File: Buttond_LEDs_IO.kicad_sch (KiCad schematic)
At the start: 16 parts, among them J14 Conn_01x04, J15 Conn_01x08, SW1 RESET, SW2 BOOT

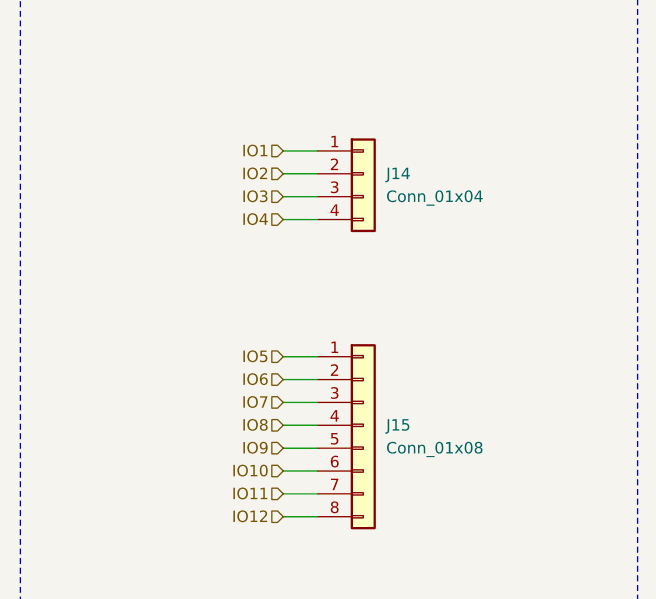
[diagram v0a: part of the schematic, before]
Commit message: moving to kicad-bild
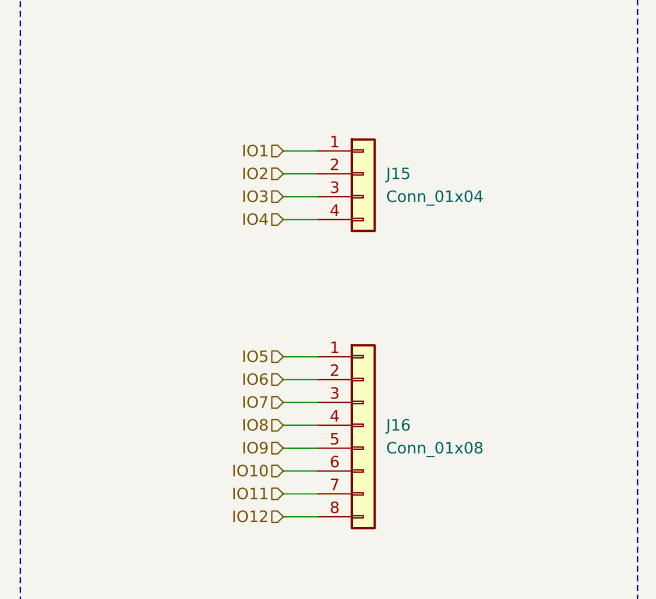
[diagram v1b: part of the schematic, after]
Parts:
- renumbered J14 to J15, J15 to J16
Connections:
- net BOOT: now also SW2.3 (B), SW2.4 (B); no longer SW2.2 (B)
- net GND: now also SW1.2 (A), SW2.2 (A)
- net Reset: now also SW1.3 (B), SW1.4 (B); no longer SW1.2 (B)
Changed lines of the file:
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@@
 		(dnp no)
 		(fields_autoplaced yes)
-		(property "Reference" "J15"
+		(property "Reference" "J16"
 			(at 247.65 90.8049 0)
 			(effects
@@
 			(project ""
 				(path "/795c8e51-3ded-4d21-b864-aaff31c5def7/6282503b-e4ab-454b-a074-f701a067f39b/cecfe08a-2de2-4171-9051-c68b429ab9e8"
-					(reference "J15")
+					(reference "J16")
 					(unit 1)
 				)
@@
 		(dnp no)
 		(fields_autoplaced yes)
-		(property "Reference" "#PWR059"
+		(property "Reference" "#PWR063"
 			(at 156.21 107.95 0)
 			(effects
@@
 			(project "VehicleControlUnit"
 				(path "/795c8e51-3ded-4d21-b864-aaff31c5def7/6282503b-e4ab-454b-a074-f701a067f39b/cecfe08a-2de2-4171-9051-c68b429ab9e8"
-					(reference "#PWR059")
+					(reference "#PWR063")
 					(unit 1)
 				)
@@
 			)
 		)
+		(property "Sim.Pins" "1=K 2=A"
+			(at 133.35 92.71 0)
+			(effects
+				(font
+					(size 1.27 1.27)
+				)
+				(hide yes)
+			)
+		)
 		(pin "1"
 		)
@@
 		(dnp no)
 		(fields_autoplaced yes)
-		(property "Reference" "J14"
+		(property "Reference" "J15"
 			(at 247.65 62.8649 0)
 			(effects
@@
 			(project ""
 				(path "/795c8e51-3ded-4d21-b864-aaff31c5def7/6282503b-e4ab-454b-a074-f701a067f39b/cecfe08a-2de2-4171-9051-c68b429ab9e8"
-					(reference "J14")
+					(reference "J15")
 					(unit 1)
 				)
@@
 			)
 		)
-		(pin "2"
-		)
-		(pin "1"
-		)
-		(pin "1"
+		(pin "4"
+		)
+		(pin "1"
+		)
+		(pin "3"
 		)
 		(pin "2"
@@
 		(dnp no)
 		(fields_autoplaced yes)
-		(property "Reference" "#PWR054"
+		(property "Reference" "#PWR058"
 			(at 60.96 121.92 0)
 			(effects
@@
 			(project "VehicleControlUnit"
 				(path "/795c8e51-3ded-4d21-b864-aaff31c5def7/6282503b-e4ab-454b-a074-f701a067f39b/cecfe08a-2de2-4171-9051-c68b429ab9e8"
-					(reference "#PWR054")
+					(reference "#PWR058")
 					(unit 1)
 				)
@@
 		(dnp no)
 		(fields_autoplaced yes)
-		(property "Reference" "#PWR060"
+		(property "Reference" "#PWR064"
 			(at 167.64 107.95 0)
 			(effects
@@
 			(project "VehicleControlUnit"
 				(path "/795c8e51-3ded-4d21-b864-aaff31c5def7/6282503b-e4ab-454b-a074-f701a067f39b/cecfe08a-2de2-4171-9051-c68b429ab9e8"
-					(reference "#PWR060")
+					(reference "#PWR064")
 					(unit 1)
 				)
@@
 		(dnp no)
 		(fields_autoplaced yes)
-		(property "Reference" "#PWR053"
+		(property "Reference" "#PWR057"
 			(at 60.96 80.01 0)
 			(effects
@@
 			(project "VehicleControlUnit"
 				(path "/795c8e51-3ded-4d21-b864-aaff31c5def7/6282503b-e4ab-454b-a074-f701a067f39b/cecfe08a-2de2-4171-9051-c68b429ab9e8"
-					(reference "#PWR053")
+					(reference "#PWR057")
 					(unit 1)
 				)
@@
 			)
 		)
+		(property "Sim.Pins" "1=K 2=A"
+			(at 144.78 92.71 0)
+			(effects
+				(font
+					(size 1.27 1.27)
+				)
+				(hide yes)
+			)
+		)
 		(pin "1"
 		)
@@
 		(dnp no)
 		(fields_autoplaced yes)
-		(property "Reference" "#PWR055"
+		(property "Reference" "#PWR059"
 			(at 80.01 80.01 0)
 			(effects
@@
 			(project "VehicleControlUnit"
 				(path "/795c8e51-3ded-4d21-b864-aaff31c5def7/6282503b-e4ab-454b-a074-f701a067f39b/cecfe08a-2de2-4171-9051-c68b429ab9e8"
-					(reference "#PWR055")
+					(reference "#PWR059")
 					(unit 1)
 				)
@@
 		(dnp no)
 		(fields_autoplaced yes)
-		(property "Reference" "#PWR057"
+		(property "Reference" "#PWR061"
 			(at 133.35 107.95 0)
 			(effects
@@
 			(project "VehicleControlUnit"
 				(path "/795c8e51-3ded-4d21-b864-aaff31c5def7/6282503b-e4ab-454b-a074-f701a067f39b/cecfe08a-2de2-4171-9051-c68b429ab9e8"
-					(reference "#PWR057")
+					(reference "#PWR061")
 					(unit 1)
 				)
@@
 	)
 	(symbol
-		(lib_name "SW_MEC_5G_1")
 		(lib_id "Switch:SW_MEC_5G")
 		(at 71.12 63.5 0)
@@
 		(pin "2"
 		)
-		(pin "1"
-		)
-		(pin "1"
-		)
-		(pin "2"
+		(pin "3"
+		)
+		(pin "1"
+		)
+		(pin "4"
 		)
 		(instances
@@
 		)
 		(property "Description" "Light emitting diode"
+			(at 167.64 92.71 0)
+			(effects
+				(font
+					(size 1.27 1.27)
+				)
+				(hide yes)
+			)
+		)
+		(property "Sim.Pins" "1=K 2=A"
 			(at 167.64 92.71 0)
 			(effects
@@
 		(dnp no)
 		(fields_autoplaced yes)
-		(property "Reference" "#PWR056"
+		(property "Reference" "#PWR060"
 			(at 80.01 121.92 0)
 			(effects
@@
 			(project "VehicleControlUnit"
 				(path "/795c8e51-3ded-4d21-b864-aaff31c5def7/6282503b-e4ab-454b-a074-f701a067f39b/cecfe08a-2de2-4171-9051-c68b429ab9e8"
-					(reference "#PWR056")
+					(reference "#PWR060")
 					(unit 1)
 				)
@@
 			)
 		)
+		(property "Sim.Pins" "1=K 2=A"
+			(at 156.21 92.71 0)
+			(effects
+				(font
+					(size 1.27 1.27)
+				)
+				(hide yes)
+			)
+		)
 		(pin "1"
 		)
@@
 		(dnp no)
 		(fields_autoplaced yes)
-		(property "Reference" "#PWR058"
+		(property "Reference" "#PWR062"
 			(at 144.78 107.95 0)
 			(effects
@@
 			(project "VehicleControlUnit"
 				(path "/795c8e51-3ded-4d21-b864-aaff31c5def7/6282503b-e4ab-454b-a074-f701a067f39b/cecfe08a-2de2-4171-9051-c68b429ab9e8"
-					(reference "#PWR058")
-					(unit 1)
-				)
+					(reference "#PWR062")
+					(unit 1)
+				)

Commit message: fuck the rats nest im doing it tomorrow
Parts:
- removed J15: Conn_01x04, Connector_PinHeader_2.54mm:PinHeader_1x04_P2.54mm_Vertical, symbol Connector_Generic:Conn_01x04
- removed J16: Conn_01x08, Connector_PinHeader_2.54mm:PinHeader_1x08_P2.54mm_Vertical, symbol Connector_Generic:Conn_01x08
- added J14, J15: SFH11-PBPC-D05-ST-BK, UTSVT_Connectors:CONN_SFH11-xxxC-D05-ST-XX_SUL, symbol UTSVT_Connectors:SFH11-PBPC-D05-ST-BK
- renumbered C16 to C17, C17 to C18, R25 to R22, R26 to R23, R27 to R24, R28 to R25, R29 to R26, R30 to R27
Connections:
- net GND: now also J14.10, J15.10
- net IO1: now also J14.1
- net IO10: now also J15.1
- net IO11: now also J15.2
- net IO12: now also J15.3
- net IO2: now also J14.2
- net IO3: now also J14.3
- net IO4: now also J14.4
- net IO5: now also J14.5
- net IO6: now also J14.6
- net IO7: now also J14.7
- net IO8: now also J14.8
- net IO9: now also J14.9
- new net IO13: J15.4
- new net USB_D+: J15.5
- new net USB_D-: J15.6
- no-connect marks 0 -> 3

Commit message: routing done
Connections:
- net USB_D+ is gone; now on net IO7: J15.5
- net USB_D- is gone; now on net IO8: J15.6
- net GND: now also J14.9, J15.9
- net IO1: now also J14.7; no longer J14.1
- net IO10: now also J15.4; no longer J15.1
- net IO11: now also J15.1; no longer J15.2
- net IO12: now also J15.2; no longer J15.3
- net IO13: now also J14.2; no longer J15.4
- net IO2: now also J14.5; no longer J14.2
- net IO4: now also J14.1; no longer J14.4
- net IO5: now also J15.7; no longer J14.5
- net IO6: now also J15.8; no longer J14.6
- net IO7: no longer J14.7
- net IO8: no longer J14.8
- net IO9: now also J15.3; no longer J14.9

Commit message: lakshay nitpicks
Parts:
- renumbered C17 to C18, C18 to C19, J14 to J12, J15 to J13
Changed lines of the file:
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@@
 		(dnp no)
 		(fields_autoplaced yes)
-		(property "Reference" "#PWR064"
+		(property "Reference" "#PWR065"
 			(at 156.21 107.95 0)
 			(effects
@@
 			(project "VehicleControlUnit"
 				(path "/795c8e51-3ded-4d21-b864-aaff31c5def7/6282503b-e4ab-454b-a074-f701a067f39b/cecfe08a-2de2-4171-9051-c68b429ab9e8"
-					(reference "#PWR064")
+					(reference "#PWR065")
 					(unit 1)
 				)
@@
 		(dnp no)
 		(fields_autoplaced yes)
-		(property "Reference" "#PWR059"
+		(property "Reference" "#PWR060"
 			(at 60.96 121.92 0)
 			(effects
@@
 			(project "VehicleControlUnit"
 				(path "/795c8e51-3ded-4d21-b864-aaff31c5def7/6282503b-e4ab-454b-a074-f701a067f39b/cecfe08a-2de2-4171-9051-c68b429ab9e8"
-					(reference "#PWR059")
+					(reference "#PWR060")
 					(unit 1)
 				)
@@
 		(dnp no)
 		(fields_autoplaced yes)
-		(property "Reference" "#PWR065"
+		(property "Reference" "#PWR066"
 			(at 167.64 107.95 0)
 			(effects
@@
 			(project "VehicleControlUnit"
 				(path "/795c8e51-3ded-4d21-b864-aaff31c5def7/6282503b-e4ab-454b-a074-f701a067f39b/cecfe08a-2de2-4171-9051-c68b429ab9e8"
-					(reference "#PWR065")
+					(reference "#PWR066")
 					(unit 1)
 				)
@@
 		(on_board yes)
 		(dnp no)
-		(property "Reference" "J14"
+		(property "Reference" "J12"
 			(at 230.505 36.83 0)
 			(effects
@@
 			(project "VehicleControlUnit"
 				(path "/795c8e51-3ded-4d21-b864-aaff31c5def7/6282503b-e4ab-454b-a074-f701a067f39b/cecfe08a-2de2-4171-9051-c68b429ab9e8"
-					(reference "J14")
+					(reference "J12")
 					(unit 1)
 				)
@@
 		(dnp no)
 		(fields_autoplaced yes)
-		(property "Reference" "C17"
+		(property "Reference" "C18"
 			(at 57.15 67.3099 0)
 			(effects
@@
 			(project "VehicleControlUnit"
 				(path "/795c8e51-3ded-4d21-b864-aaff31c5def7/6282503b-e4ab-454b-a074-f701a067f39b/cecfe08a-2de2-4171-9051-c68b429ab9e8"
-					(reference "C17")
+					(reference "C18")
 					(unit 1)
 				)
@@
 		(dnp no)
 		(fields_autoplaced yes)
-		(property "Reference" "#PWR058"
+		(property "Reference" "#PWR059"
 			(at 60.96 80.01 0)
 			(effects
@@
 			(project "VehicleControlUnit"
 				(path "/795c8e51-3ded-4d21-b864-aaff31c5def7/6282503b-e4ab-454b-a074-f701a067f39b/cecfe08a-2de2-4171-9051-c68b429ab9e8"
-					(reference "#PWR058")
+					(reference "#PWR059")
 					(unit 1)
 				)
@@
 		(dnp no)
 		(fields_autoplaced yes)
-		(property "Reference" "#PWR060"
+		(property "Reference" "#PWR061"
 			(at 80.01 80.01 0)
 			(effects
@@
 			(project "VehicleControlUnit"
 				(path "/795c8e51-3ded-4d21-b864-aaff31c5def7/6282503b-e4ab-454b-a074-f701a067f39b/cecfe08a-2de2-4171-9051-c68b429ab9e8"
-					(reference "#PWR060")
+					(reference "#PWR061")
 					(unit 1)
 				)
@@
 		(dnp no)
 		(fields_autoplaced yes)
-		(property "Reference" "#PWR066"
+		(property "Reference" "#PWR068"
 			(at 238.125 73.025 0)
 			(effects
@@
 			(project "VehicleControlUnit"
 				(path "/795c8e51-3ded-4d21-b864-aaff31c5def7/6282503b-e4ab-454b-a074-f701a067f39b/cecfe08a-2de2-4171-9051-c68b429ab9e8"
-					(reference "#PWR066")
+					(reference "#PWR068")
 					(unit 1)
 				)
@@
 		(on_board yes)
 		(dnp no)
-		(property "Reference" "J15"
+		(property "Reference" "J13"
 			(at 230.505 74.93 0)
 			(effects
@@
 			(project "VehicleControlUnit"
 				(path "/795c8e51-3ded-4d21-b864-aaff31c5def7/6282503b-e4ab-454b-a074-f701a067f39b/cecfe08a-2de2-4171-9051-c68b429ab9e8"
-					(reference "J15")
+					(reference "J13")
 					(unit 1)
 				)
@@
 		(dnp no)
 		(fields_autoplaced yes)
-		(property "Reference" "#PWR062"
+		(property "Reference" "#PWR063"
 			(at 133.35 107.95 0)
 			(effects
@@
 			(project "VehicleControlUnit"
 				(path "/795c8e51-3ded-4d21-b864-aaff31c5def7/6282503b-e4ab-454b-a074-f701a067f39b/cecfe08a-2de2-4171-9051-c68b429ab9e8"
-					(reference "#PWR062")
+					(reference "#PWR063")
 					(unit 1)
 				)
@@
 		(dnp no)
 		(fields_autoplaced yes)
-		(property "Reference" "#PWR061"
+		(property "Reference" "#PWR062"
 			(at 80.01 121.92 0)
 			(effects
@@
 			(project "VehicleControlUnit"
 				(path "/795c8e51-3ded-4d21-b864-aaff31c5def7/6282503b-e4ab-454b-a074-f701a067f39b/cecfe08a-2de2-4171-9051-c68b429ab9e8"
-					(reference "#PWR061")
+					(reference "#PWR062")
 					(unit 1)
 				)
@@
 		(dnp no)
 		(fields_autoplaced yes)
-		(property "Reference" "#PWR063"
+		(property "Reference" "#PWR064"
 			(at 144.78 107.95 0)
 			(effects
@@
 			(project "VehicleControlUnit"
 				(path "/795c8e51-3ded-4d21-b864-aaff31c5def7/6282503b-e4ab-454b-a074-f701a067f39b/cecfe08a-2de2-4171-9051-c68b429ab9e8"
-					(reference "#PWR063")
+					(reference "#PWR064")
 					(unit 1)
 				)
@@
 		(dnp no)
 		(fields_autoplaced yes)
-		(property "Reference" "C18"
+		(property "Reference" "C19"
 			(at 57.15 109.2199 0)
 			(effects
@@
 			(project "VehicleControlUnit"
 				(path "/795c8e51-3ded-4d21-b864-aaff31c5def7/6282503b-e4ab-454b-a074-f701a067f39b/cecfe08a-2de2-4171-9051-c68b429ab9e8"
-					(reference "C18")
-					(unit 1)
-				)
+					(reference "C19")
+					(unit 1)
+				)

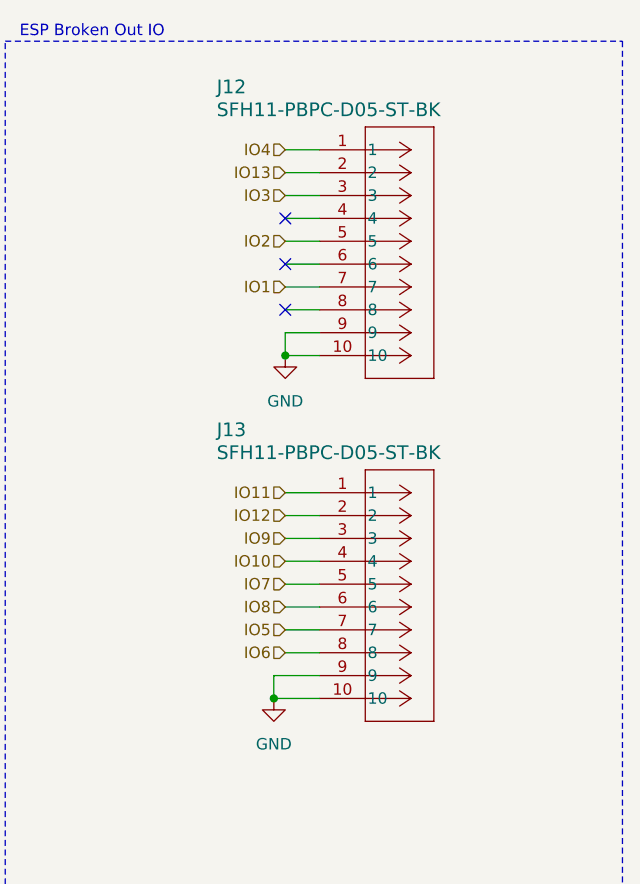
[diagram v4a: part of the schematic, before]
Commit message: replaced 0805 with 0603, changed logic analyzer symbol and silkscreen
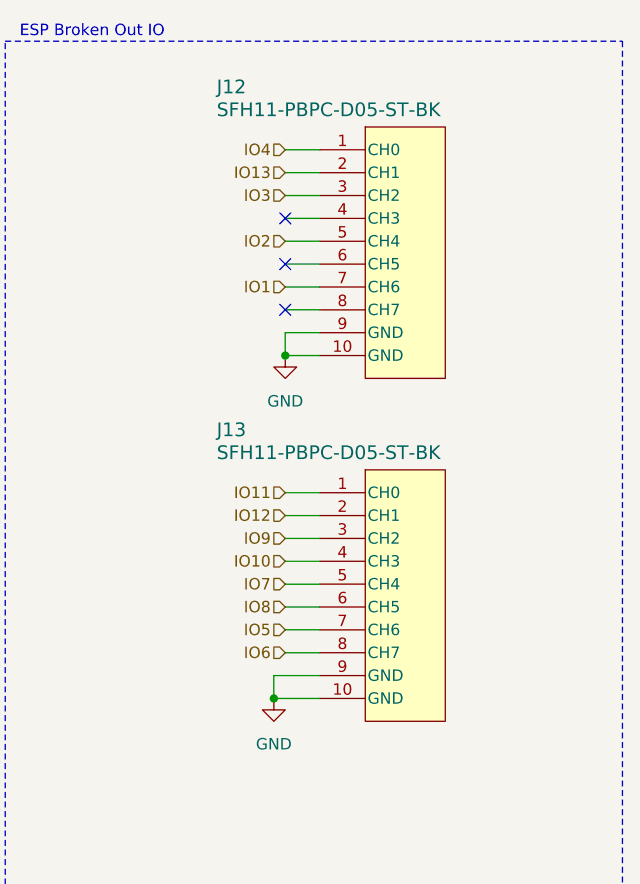
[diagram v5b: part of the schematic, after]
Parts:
- C18, C19: footprint Capacitor_SMD:C_0805_2012Metric -> Capacitor_SMD:C_0603_1608Metric
- LV1, LV2, LV3, LV4: footprint LED_SMD:LED_0805_2012Metric -> LED_SMD:LED_0603_1608Metric
- R22, R23, R24, R25, R26, R27: footprint Resistor_SMD:R_0805_2012Metric -> Resistor_SMD:R_0603_1608Metric
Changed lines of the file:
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@@
 			)
 		)
-		(property "Footprint" "LED_SMD:LED_0805_2012Metric"
+		(property "Footprint" "LED_SMD:LED_0603_1608Metric"
 			(at 133.35 92.71 0)
 			(effects
@@
 			)
 		)
-		(property "Footprint" "Resistor_SMD:R_0805_2012Metric"
+		(property "Footprint" "Resistor_SMD:R_0603_1608Metric"
 			(at 134.366 84.074 90)
 			(effects
@@
 			)
 		)
-		(property "Footprint" "Capacitor_SMD:C_0805_2012Metric"
+		(property "Footprint" "Capacitor_SMD:C_0603_1608Metric"
 			(at 59.9948 72.39 0)
 			(effects
@@
 			)
 		)
-		(property "Footprint" "Resistor_SMD:R_0805_2012Metric"
+		(property "Footprint" "Resistor_SMD:R_0603_1608Metric"
 			(at 59.944 56.134 90)
 			(effects
@@
 			)
 		)
-		(property "Footprint" "Resistor_SMD:R_0805_2012Metric"
+		(property "Footprint" "Resistor_SMD:R_0603_1608Metric"
 			(at 145.796 84.074 90)
 			(effects
@@
 			)
 		)
-		(property "Footprint" "LED_SMD:LED_0805_2012Metric"
+		(property "Footprint" "LED_SMD:LED_0603_1608Metric"
 			(at 144.78 92.71 0)
 			(effects
@@
 			)
 		)
-		(property "Footprint" "Resistor_SMD:R_0805_2012Metric"
+		(property "Footprint" "Resistor_SMD:R_0603_1608Metric"
 			(at 157.226 84.074 90)
 			(effects
@@
 	)
 	(symbol
+		(lib_name "SFH11-PBPC-D05-ST-BK_1")
 		(lib_id "UTSVT_Connectors:SFH11-PBPC-D05-ST-BK")
 		(at 241.935 81.915 0)
@@
 			)
 		)
-		(property "Footprint" "Resistor_SMD:R_0805_2012Metric"
+		(property "Footprint" "Resistor_SMD:R_0603_1608Metric"
 			(at 168.656 84.074 90)
 			(effects
@@
 			)
 		)
-		(property "Footprint" "LED_SMD:LED_0805_2012Metric"
+		(property "Footprint" "LED_SMD:LED_0603_1608Metric"
 			(at 167.64 92.71 0)
 			(effects
@@
 			)
 		)
-		(property "Footprint" "LED_SMD:LED_0805_2012Metric"
+		(property "Footprint" "LED_SMD:LED_0603_1608Metric"
 			(at 156.21 92.71 0)
 			(effects
@@
 			)
 		)
-		(property "Footprint" "Resistor_SMD:R_0805_2012Metric"
+		(property "Footprint" "Resistor_SMD:R_0603_1608Metric"
 			(at 59.944 98.044 90)
 			(effects
@@
 			)
 		)
-		(property "Footprint" "Capacitor_SMD:C_0805_2012Metric"
+		(property "Footprint" "Capacitor_SMD:C_0603_1608Metric"
 			(at 59.9948 114.3 0)
 			(effects
